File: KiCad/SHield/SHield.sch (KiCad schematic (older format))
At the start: 18 parts, among them J1 Conn_01x08_Female, J2 Conn_01x04_Female, J3 Conn_01x04_Female, P1 Power, P2 Analog, P3 Digital, P4 Digital, P5 CONN_01X01, P6 CONN_01X01, P7 CONN_01X01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

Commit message: ajout shield capteur gaz SB
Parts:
- D1: footprint LED_THT:LED_D3.0mm -> LED_THT:LED_D5.0mm_FlatTop
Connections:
- net 11(**/MOSI): now also J1.1 (Pin_1); no longer J1.2 (Pin_2)
- net 12(MISO): now also J1.2 (Pin_2); no longer J1.1 (Pin_1)
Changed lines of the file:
@@
 	0    -1   -1   0
 $EndComp
+Text Label 2900 1600 2    60   ~ 0
+11(**/MOSI)
 Text Label 2900 1700 2    60   ~ 0
-11(**/MOSI)
-Text Label 2900 1600 2    60   ~ 0
 12(MISO)
 Text Label 2900 2000 2    60   ~ 0
@@
 F 0 "D1" H 7342 1545 50  0000 C CNN
 F 1 "LED" H 7342 1636 50  0000 C CNN
-F 2 "LED_THT:LED_D3.0mm" H 7350 1800 50  0001 C CNN
+F 2 "LED_THT:LED_D5.0mm_FlatTop" H 7350 1800 50  0001 C CNN
 F 3 "~" H 7350 1800 50  0001 C CNN
 	1    7350 1800

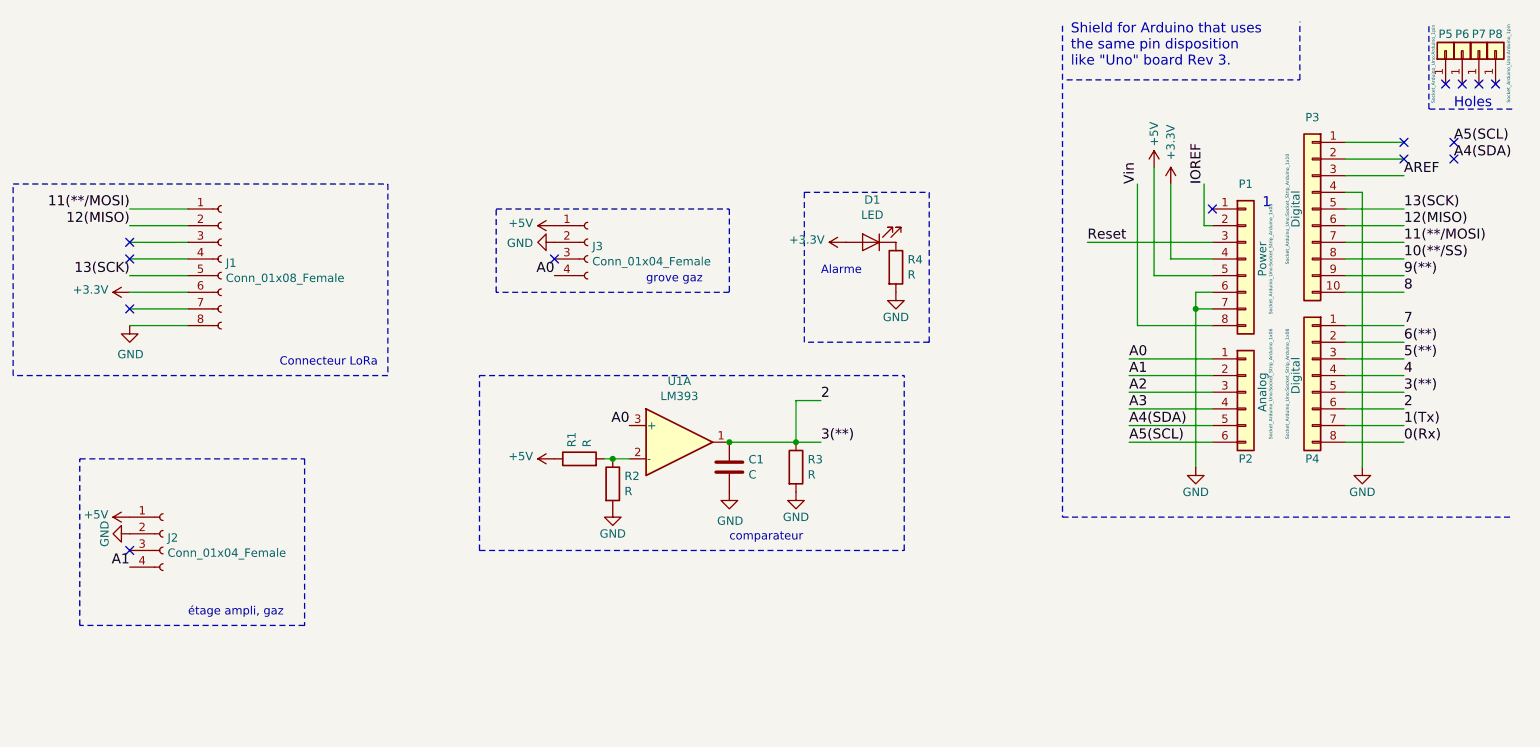
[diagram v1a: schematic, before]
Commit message: modification et ajout carte pour capteur en salle blanche
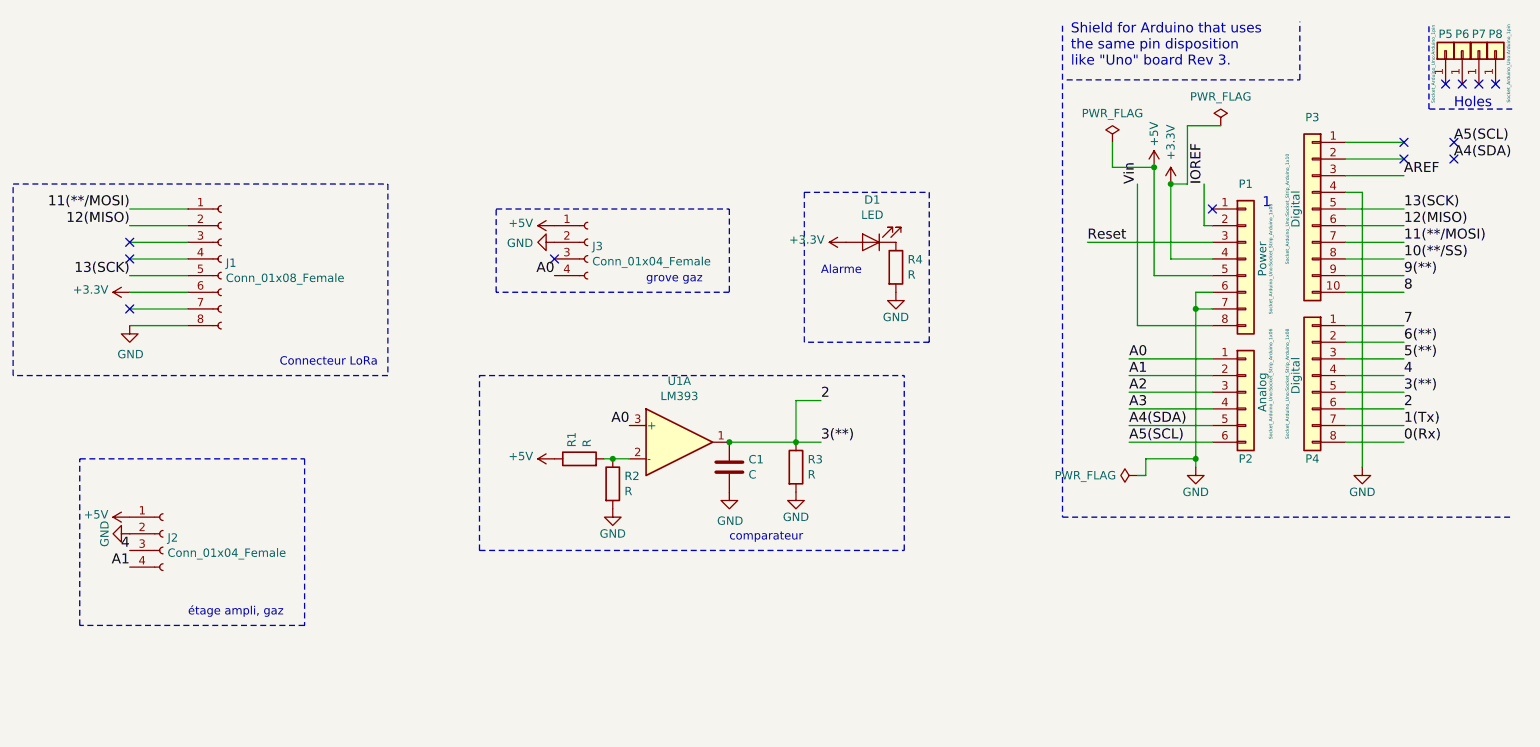
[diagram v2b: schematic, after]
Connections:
- net 4: now also J2.3 (Pin_3)
- no-connect marks 14 -> 13
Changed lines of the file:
@@
 	9300 2100 9300 2200
 Wire Wire Line
-	9300 2200 9300 3150
+	9300 2200 9300 3100
 Wire Notes Line
 	8500 500  8500 3450
@@
 Text Label 2900 3750 2    60   ~ 0
 A1
-$Comp
-L power:+5V #PWR0103
-U 1 1 5BC93F7B
-P 2900 3450
-F 0 "#PWR0103" H 2900 3300 50  0001 C CNN
-F 1 "+5V" V 2915 3578 50  0000 L CNN
-F 2 "" H 2900 3450 50  0001 C CNN
-F 3 "" H 2900 3450 50  0001 C CNN
-	1    2900 3450
-	0    -1   -1   0
-$EndComp
 Wire Notes Line
 	2600 3100 3950 3100
@@
 	0    1    1    0
 $EndComp
-NoConn ~ 2900 3650
 Text Label 10850 1200 0    60   ~ 0
 A5(SCL)
@@
 Wire Notes Line
 	5000 3650 7550 3650
+Text Label 2900 3650 2    60   ~ 0
+4
+$Comp
+L power:+5V #PWR?
+U 1 1 5BE1A15D
+P 2900 3450
+F 0 "#PWR?" H 2900 3300 50  0001 C CNN
+F 1 "+5V" V 2915 3578 50  0000 L CNN
+F 2 "" H 2900 3450 50  0001 C CNN
+F 3 "" H 2900 3450 50  0001 C CNN
+	1    2900 3450
+	0    -1   -1   0
+$EndComp
+$Comp
+L power:PWR_FLAG #FLG?
+U 1 1 5BE16345
+P 8800 1200
+F 0 "#FLG?" H 8800 1275 50  0001 C CNN
+F 1 "PWR_FLAG" H 8800 1374 50  0000 C CNN
+F 2 "" H 8800 1200 50  0001 C CNN
+F 3 "~" H 8800 1200 50  0001 C CNN
+	1    8800 1200
+	1    0    0    -1
+$EndComp
+$Comp
+L power:PWR_FLAG #FLG?
+U 1 1 5BE1638B
+P 9450 1100
+F 0 "#FLG?" H 9450 1175 50  0001 C CNN
+F 1 "PWR_FLAG" H 9450 1274 50  0000 C CNN
+F 2 "" H 9450 1100 50  0001 C CNN
+F 3 "~" H 9450 1100 50  0001 C CNN
+	1    9450 1100
+	1    0    0    -1
+$EndComp
+$Comp
+L power:PWR_FLAG #FLG?
+U 1 1 5BE163D1
+P 8950 3200
+F 0 "#FLG?" H 8950 3275 50  0001 C CNN
+F 1 "PWR_FLAG" V 8950 3328 50  0000 L CNN
+F 2 "" H 8950 3200 50  0001 C CNN
+F 3 "~" H 8950 3200 50  0001 C CNN
+	1    8950 3200
+	0    -1   -1   0
+$EndComp
+Wire Wire Line
+	8950 3200 9000 3200
+Wire Wire Line
+	9000 3200 9000 3100
+Wire Wire Line
+	9000 3100 9300 3100
+Connection ~ 9300 3100
+Wire Wire Line
+	9300 3100 9300 3150
+Wire Wire Line
+	8800 1200 8800 1350
+Wire Wire Line
+	8800 1350 9050 1350
+Connection ~ 9050 1350
+Wire Wire Line
+	9150 1450 9250 1450
+Wire Wire Line
+	9250 1450 9250 1100
+Wire Wire Line
+	9250 1100 9450 1100
+Connection ~ 9150 1450
 $EndSCHEMATC

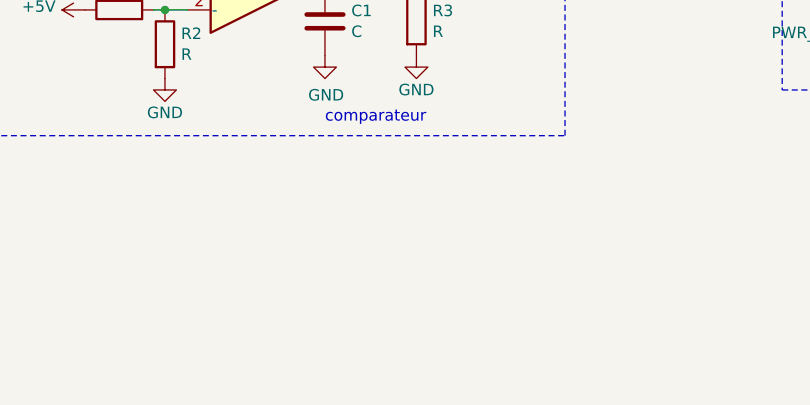
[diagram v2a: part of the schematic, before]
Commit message: Modifications deu shield, ajout de deux LED
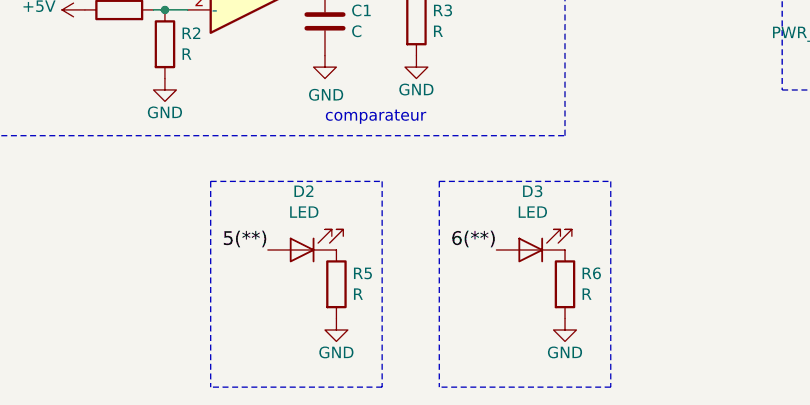
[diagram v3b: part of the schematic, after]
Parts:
- added D2, D3: LED, LED_THT:LED_D3.0mm_FlatTop, symbol Device:LED
- added R5, R6: R, Resistor_THT:R_Axial_DIN0204_L3.6mm_D1.6mm_P5.08mm_Horizontal, symbol Device:R
- D1: footprint LED_THT:LED_D5.0mm_FlatTop -> LED_THT:LED_D3.0mm_FlatTop
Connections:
- net 5(**): now also D2.2 (A)
- net 6(**): now also D3.2 (A)
- net GND: now also R5.2, R6.2
- new net: D3.1 (K), R6.1
- new net: D2.1 (K), R5.1
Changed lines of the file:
@@
 F 0 "D1" H 7342 1545 50  0000 C CNN
 F 1 "LED" H 7342 1636 50  0000 C CNN
-F 2 "LED_THT:LED_D5.0mm_FlatTop" H 7350 1800 50  0001 C CNN
+F 2 "LED_THT:LED_D3.0mm_FlatTop" H 7350 1800 50  0001 C CNN
 F 3 "~" H 7350 1800 50  0001 C CNN
 	1    7350 1800
@@
 4
 $Comp
-L power:+5V #PWR?
+L power:+5V #PWR0103
 U 1 1 5BE1A15D
 P 2900 3450
-F 0 "#PWR?" H 2900 3300 50  0001 C CNN
+F 0 "#PWR0103" H 2900 3300 50  0001 C CNN
 F 1 "+5V" V 2915 3578 50  0000 L CNN
 F 2 "" H 2900 3450 50  0001 C CNN
@@
 $EndComp
 $Comp
-L power:PWR_FLAG #FLG?
+L power:PWR_FLAG #FLG0101
 U 1 1 5BE16345
 P 8800 1200
-F 0 "#FLG?" H 8800 1275 50  0001 C CNN
+F 0 "#FLG0101" H 8800 1275 50  0001 C CNN
 F 1 "PWR_FLAG" H 8800 1374 50  0000 C CNN
 F 2 "" H 8800 1200 50  0001 C CNN
@@
 $EndComp
 $Comp
-L power:PWR_FLAG #FLG?
+L power:PWR_FLAG #FLG0102
 U 1 1 5BE1638B
 P 9450 1100
-F 0 "#FLG?" H 9450 1175 50  0001 C CNN
+F 0 "#FLG0102" H 9450 1175 50  0001 C CNN
 F 1 "PWR_FLAG" H 9450 1274 50  0000 C CNN
 F 2 "" H 9450 1100 50  0001 C CNN
@@
 $EndComp
 $Comp
-L power:PWR_FLAG #FLG?
+L power:PWR_FLAG #FLG0103
 U 1 1 5BE163D1
 P 8950 3200
-F 0 "#FLG?" H 8950 3275 50  0001 C CNN
+F 0 "#FLG0103" H 8950 3275 50  0001 C CNN
 F 1 "PWR_FLAG" V 8950 3328 50  0000 L CNN
 F 2 "" H 8950 3200 50  0001 C CNN
@@
 	9250 1100 9450 1100
 Connection ~ 9150 1450
+$Comp
+L Device:LED D3
+U 1 1 5BE3138F
+P 7400 4150
+F 0 "D3" H 7392 3895 50  0000 C CNN
+F 1 "LED" H 7392 3986 50  0000 C CNN
+F 2 "LED_THT:LED_D3.0mm_FlatTop" H 7400 4150 50  0001 C CNN
+F 3 "~" H 7400 4150 50  0001 C CNN
+	1    7400 4150
+	-1   0    0    1
+$EndComp
+$Comp
+L power:GND #PWR0113
+U 1 1 5BE31396
+P 7550 4450
+F 0 "#PWR0113" H 7550 4200 50  0001 C CNN
+F 1 "GND" H 7550 4300 50  0000 C CNN
+F 2 "" H 7550 4450 50  0000 C CNN
+F 3 "" H 7550 4450 50  0000 C CNN
+	1    7550 4450
+	1    0    0    -1
+$EndComp
+Wire Notes Line
+	7000 3850 7750 3850
+$Comp
+L Device:R R6
+U 1 1 5BE3139E
+P 7550 4300
+F 0 "R6" H 7620 4346 50  0000 L CNN
+F 1 "R" H 7620 4255 50  0000 L CNN
+F 2 "Resistor_THT:R_Axial_DIN0204_L3.6mm_D1.6mm_P5.08mm_Horizontal" V 7480 4300 50  0001 C CNN
+F 3 "~" H 7550 4300 50  0001 C CNN
+	1    7550 4300
+	1    0    0    -1
+$EndComp
+Wire Notes Line
+	7750 3850 7750 4750
+Wire Notes Line
+	7750 4750 7000 4750
+Wire Notes Line
+	7000 3850 7000 4750
+$Comp
+L Device:LED D2
+U 1 1 5BE32F30
+P 6400 4150
+F 0 "D2" H 6392 3895 50  0000 C CNN
+F 1 "LED" H 6392 3986 50  0000 C CNN
+F 2 "LED_THT:LED_D3.0mm_FlatTop" H 6400 4150 50  0001 C CNN
+F 3 "~" H 6400 4150 50  0001 C CNN
+	1    6400 4150
+	-1   0    0    1
+$EndComp
+$Comp
+L power:GND #PWR0114
+U 1 1 5BE32F37
+P 6550 4450
+F 0 "#PWR0114" H 6550 4200 50  0001 C CNN
+F 1 "GND" H 6550 4300 50  0000 C CNN
+F 2 "" H 6550 4450 50  0000 C CNN
+F 3 "" H 6550 4450 50  0000 C CNN
+	1    6550 4450
+	1    0    0    -1
+$EndComp
+Wire Notes Line
+	6000 3850 6750 3850
+$Comp
+L Device:R R5
+U 1 1 5BE32F3F
+P 6550 4300
+F 0 "R5" H 6620 4346 50  0000 L CNN
+F 1 "R" H 6620 4255 50  0000 L CNN
+F 2 "Resistor_THT:R_Axial_DIN0204_L3.6mm_D1.6mm_P5.08mm_Horizontal" V 6480 4300 50  0001 C CNN
+F 3 "~" H 6550 4300 50  0001 C CNN
+	1    6550 4300
+	1    0    0    -1
+$EndComp
+Wire Notes Line
+	6750 3850 6750 4750
+Wire Notes Line
+	6750 4750 6000 4750
+Wire Notes Line
+	6000 3850 6000 4750
+Text Label 6250 4150 2    60   ~ 0
+5(**)
+Text Label 7250 4150 2    60   ~ 0
+6(**)
 $EndSCHEMATC
